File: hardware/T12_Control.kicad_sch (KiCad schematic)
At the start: 43 parts, among them J1 Screw_Terminal_01x02, J2 GX12-5M, J3 SPI LCD, J4 I2C LCD, J5 SWD, J6 Serial, Q1 TPC8107, Q2 BC817, U1 SPX2954M3-3.3_SOT223, U2 24LC32, U3 SGM8551XN, U4 STM32F103CBTx

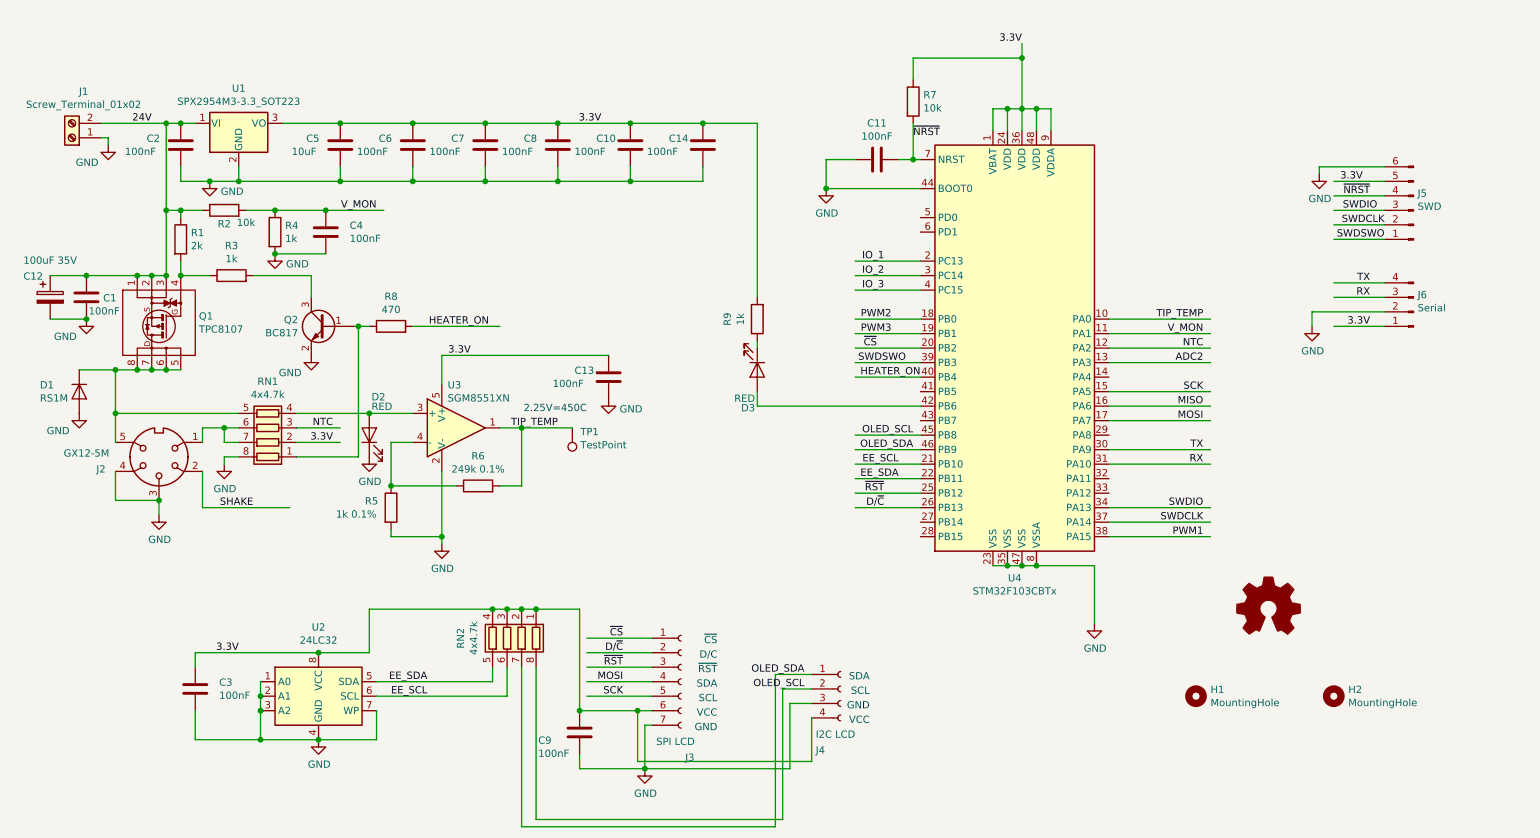
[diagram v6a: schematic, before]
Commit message: Improve power supply filtering.
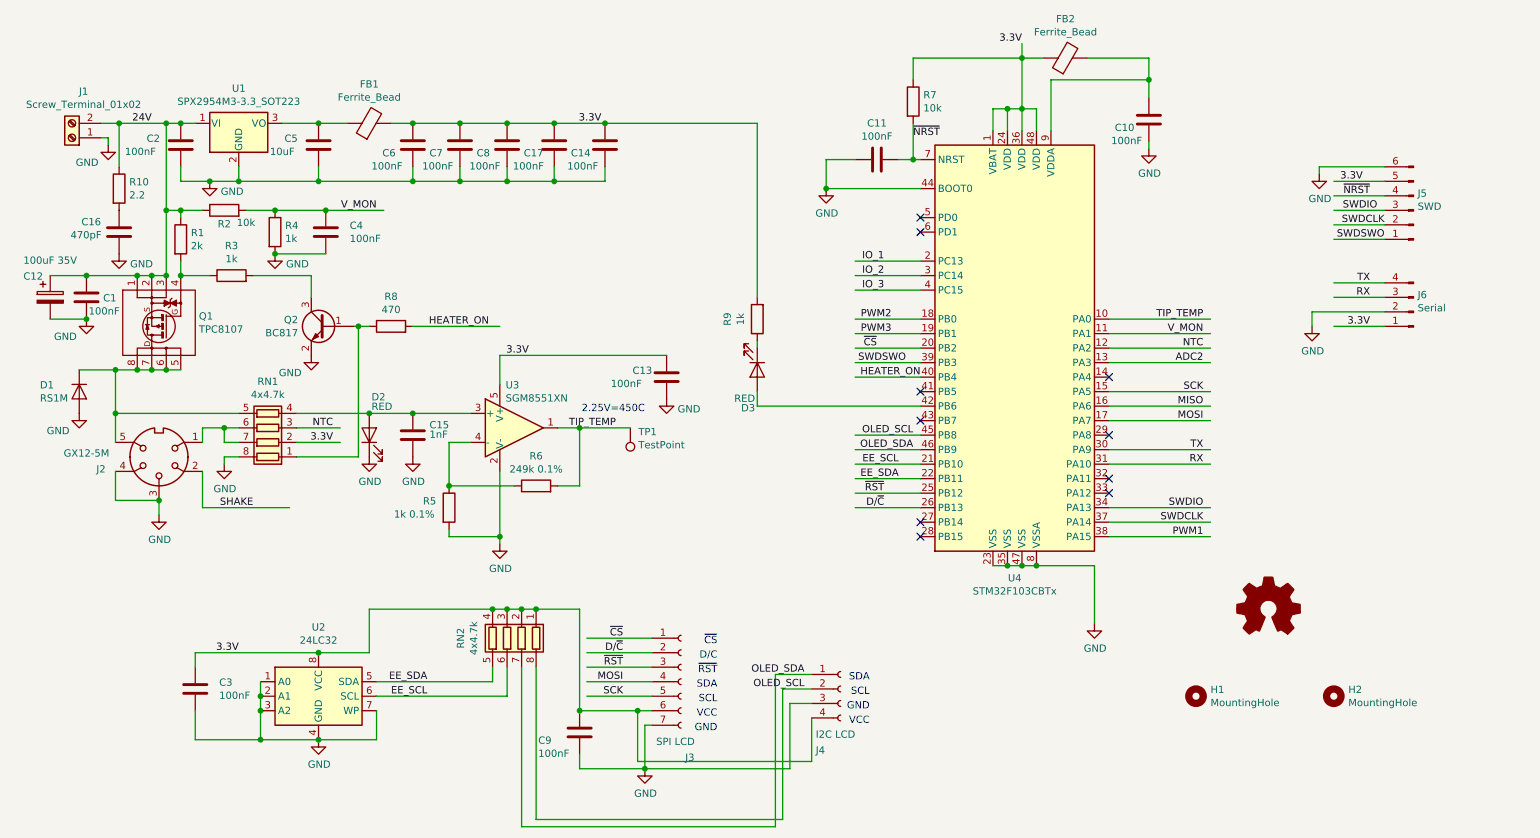
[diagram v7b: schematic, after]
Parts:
- added C15: 1nF, Capacitor_SMD:C_0603_1608Metric, symbol Device:C
- added C16: 470pF, Capacitor_SMD:C_0603_1608Metric, symbol Device:C
- added C17: 100nF, Capacitor_SMD:C_0603_1608Metric, symbol Device:C
- added FB1, FB2: Ferrite_Bead, Inductor_SMD:L_0805_2012Metric, symbol Device:Ferrite_Bead
- added R10: 2.2, Resistor_SMD:R_0603_1608Metric, symbol Device:R
- C12: footprint Capacitor_SMD:CP_Elec_6.3x7.7 -> Capacitor_THT:CP_Radial_D10.0mm_P5.00mm
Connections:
- net 24V: now also R10.1
- net 3.3V: now also C17.1, FB1.2, FB2.1; no longer C10.1, C5.1, U1.3 (VO), U4.9 (VDDA)
- net GND: now also C15.2, C16.2, C17.2
- net at D2.2 (A), RN1.4 (R4.1), U3.3 (+): now also C15.1
- new net: C16.1, R10.2
- new net: C5.1, FB1.1, U1.3 (VO)
- new net: C10.1, FB2.2, U4.9 (VDDA)
- no-connect marks 0 -> 10
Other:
- moved on the sheet: C10, C13, C14, C5, C7, C8, R5, R6, TP1, U3

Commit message: Added more ferrite beads to critical power lines.
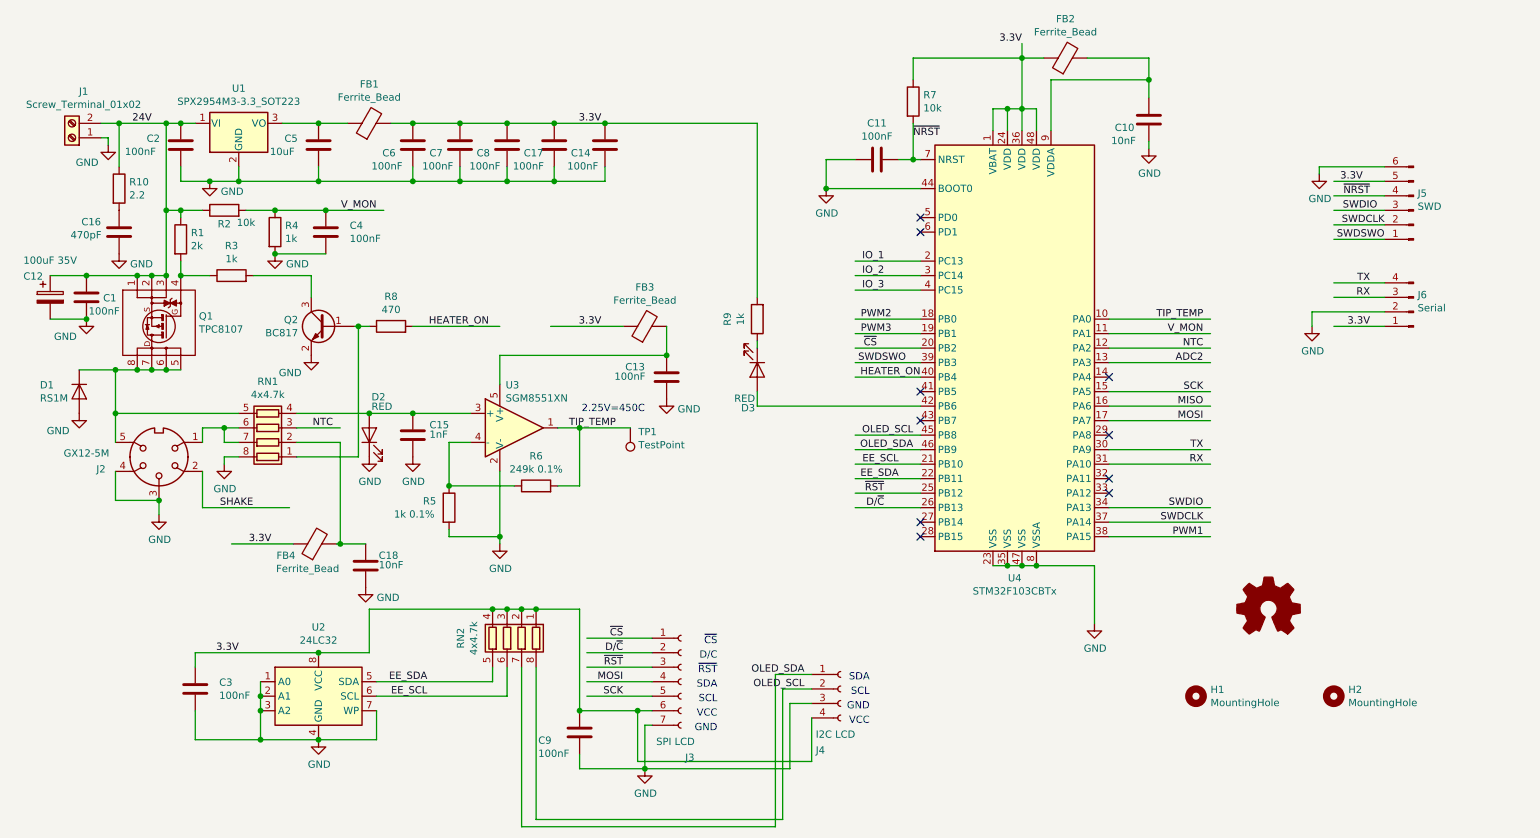
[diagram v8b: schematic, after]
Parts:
- added C18: 10nF, Capacitor_SMD:C_0603_1608Metric, symbol Device:C
- added FB3, FB4: Ferrite_Bead, Inductor_SMD:L_0805_2012Metric, symbol Device:Ferrite_Bead
- C10: value 100nF -> 10nF; LCSC Part# C14663 -> C57112
- C15: LCSC Part# C14663 -> C1588
- C16: LCSC Part# C14663 -> C1620
- FB1, FB2: LCSC Part# (none) -> C1017
- Q2: LCSC Part# (none) -> C20526
- R10: LCSC Part# C22975 -> C22939
- R3, R4, R9: LCSC Part# C22975 -> C21190
- R5: LCSC Part# C22975 -> C54019
- R6: LCSC Part# C22918 -> C95223
- R8: LCSC Part# (none) -> C23179
- RN1, RN2: LCSC Part# C181126 -> C29586
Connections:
- net 3.3V: now also FB3.1, FB4.1; no longer C13.1, RN1.2 (R2.1), U3.5 (V+)
- net GND: now also C18.2
- new net: C18.1, FB4.2, RN1.2 (R2.1)
- new net: C13.1, FB3.2, U3.5 (V+)
